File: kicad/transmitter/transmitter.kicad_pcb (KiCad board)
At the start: 2 copper layers, 69.9 x 43.2 mm, 30 parts, among them J1 Conn_01x02, J2 Conn_01x04, J3 AudioJack3, J4 AudioJack3, SW1 SW_SPST, SW2 SW_SPST, U1 ATmega328P-PU, U2 NRF24L01_Breakout, U3 MH-M18, U4 MSGEQ7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

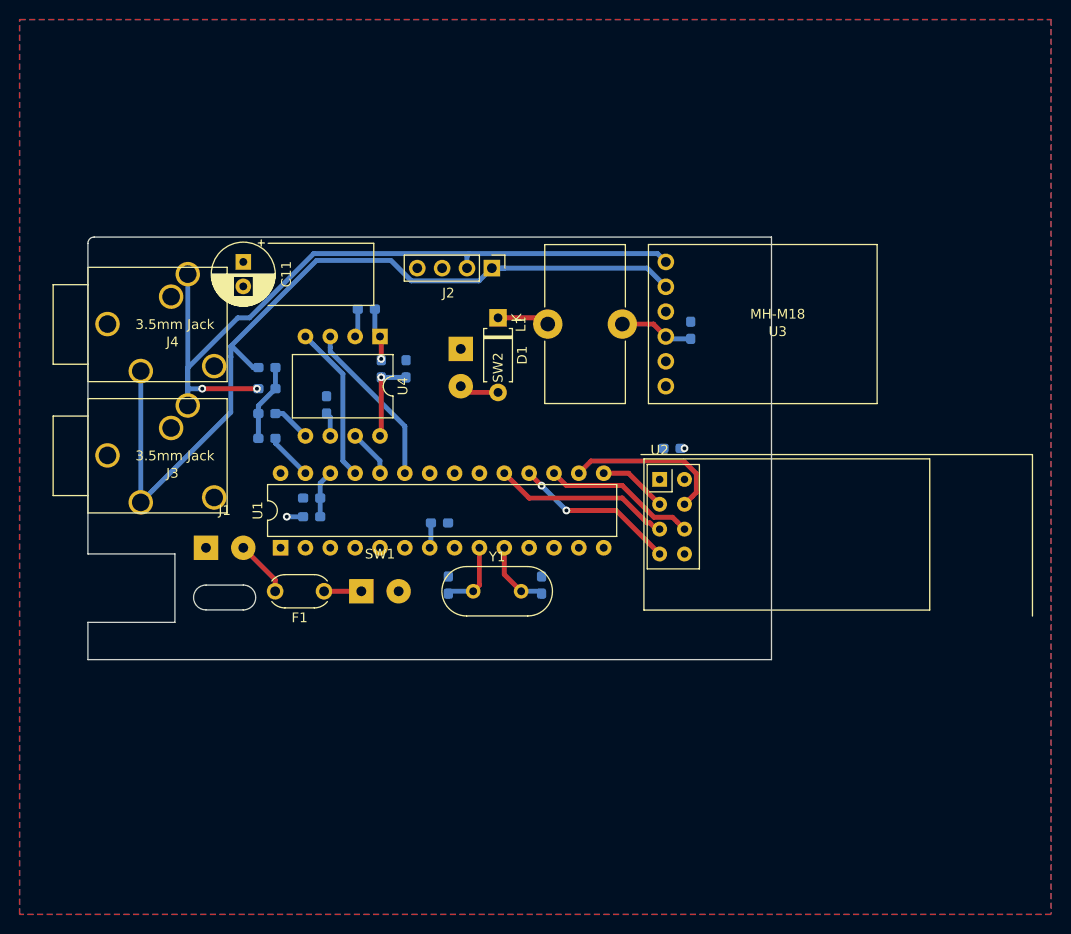
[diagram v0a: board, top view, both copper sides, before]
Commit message: Button, LEDs, ICSP header
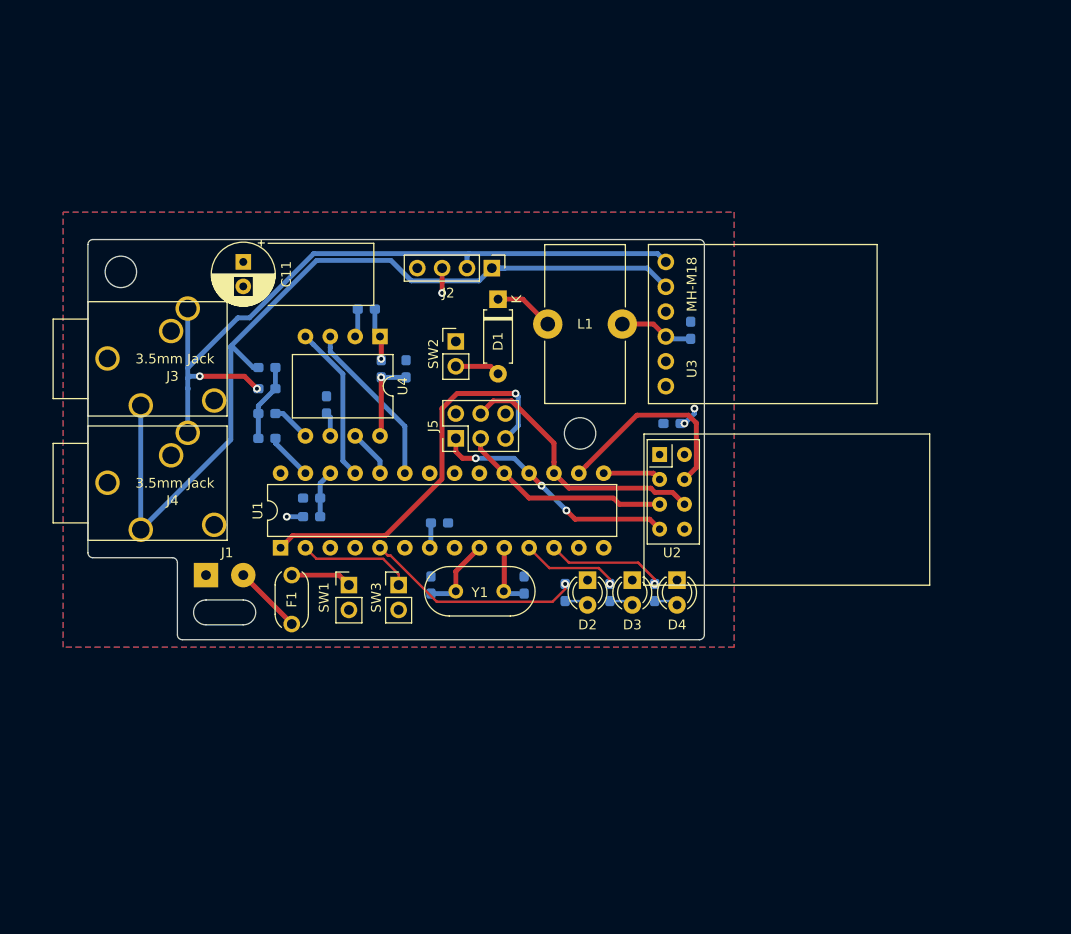
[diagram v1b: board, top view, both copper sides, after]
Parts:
- added D2: LED, LED_THT:LED_D3.0mm, F.Cu at (129.8, 87.1)
- added D3: LED, LED_THT:LED_D3.0mm, F.Cu at (134.4, 87.1)
- added D4: LED, LED_THT:LED_D3.0mm, F.Cu at (138.9, 87.1)
- added J5: Conn_02x03_Odd_Even, Connector_PinHeader_2.54mm:PinHeader_2x03_P2.54mm_Vertical, F.Cu at (116.3, 72.6)
- added R6: R, Resistor_SMD:R_0603_1608Metric_Pad1.05x0.95mm_HandSolder, B.Cu at (127.5, 88.4)
- added R7: R, Resistor_SMD:R_0603_1608Metric_Pad1.05x0.95mm_HandSolder, B.Cu at (132.1, 88.4)
- added R8: R, Resistor_SMD:R_0603_1608Metric_Pad1.05x0.95mm_HandSolder, B.Cu at (136.7, 88.4)
- added SW3: SW_Push, Connector_PinHeader_2.54mm:PinHeader_1x02_P2.54mm_Vertical, F.Cu at (110.5, 87.6)
- SW1, SW2: footprint Connector_Wire:SolderWirePad_1x02_P3.81mm_Drill1mm -> Connector_PinHeader_2.54mm:PinHeader_1x02_P2.54mm_Vertical
- moved J4 16.2 mm to (78.7, 71.4)
- moved J3 9.91 mm to (78.7, 58.7)
- moved F1 3.69 mm to (99.6, 86.6), turned to 270 degrees
- moved J1 2.79 mm to (90.8, 86.6)
- moved C4 2.54 mm to (138.4, 71.1)
- moved U2 2.54 mm to (137.2, 74.3)
- moved D1 1.91 mm to (120.7, 58.4)
- moved C3 1.78 mm to (123.3, 87.6)
- moved Y1 1.78 mm to (116.3, 88.3)
- moved C2 1.78 mm to (113.8, 87.6)
- moved SW1 1.42 mm to (105.4, 87.6)
- moved SW2 0.92 mm to (116.3, 62.7), turned to 0 degrees
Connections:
- net Radio3 renamed MOSI
- net Radio4 renamed MISO
- U1 pad 1: Net-(U1-Pad1) -> RST
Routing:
- net RST: track 0.00 -> 40.0 mm, vias 0 -> 1
- net Net-(R6-Pad1): track 0.00 -> 22.4 mm, vias 0 -> 1
- net Net-(R8-Pad1): track 0.00 -> 12.1 mm, vias 0 -> 1
- net MOSI: track 15.7 -> 27.5 mm
- net Net-(SW3-Pad1): track 0.00 -> 11.7 mm
- net Net-(R7-Pad1): track 0.00 -> 10.1 mm, vias 0 -> 1
- net MISO: track 16.8 -> 25.5 mm, vias 2 -> 3
- net Radio2: track 16.7 -> 21.1 mm
- net Net-(J2-Pad2): track 80.1 -> 76.2 mm
- net Radio5: track 18.2 -> 22.1 mm
- net GND: track 2.91 -> 5.45 mm, vias 0 -> 1
- net Net-(F1-Pad1): track 3.81 -> 6.26 mm
- net Net-(D2-Pad2): track 0.00 -> 2.45 mm
- net Net-(D4-Pad2): track 0.00 -> 2.45 mm
- net Net-(D3-Pad2): track 0.00 -> 2.45 mm
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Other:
- board size 69.9 x 43.2 mm -> 63 x 40.9 mm

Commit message: Tidy-ups pre-order
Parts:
- added REF**: OSHW-Logo2_9.8x8mm_SilkScreen, Symbol:OSHW-Logo2_9.8x8mm_SilkScreen, B.Cu at (129.5, 65.5)
- added REF**: OSHW-Logo2_9.8x8mm_SilkScreen, Symbol:OSHW-Logo2_9.8x8mm_SilkScreen, F.Cu at (0.00, 0.00)
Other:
- board size 63 x 40.9 mm -> 63 x 40.6 mm
- board text added: "Audio Lighting Transmitter v1.0 Damian Moore 2020"

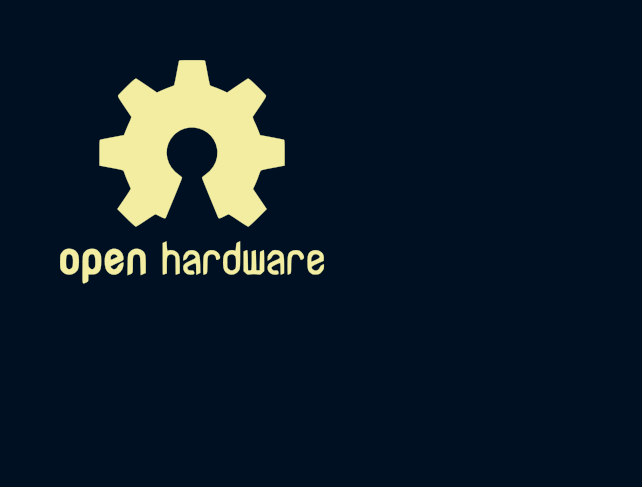
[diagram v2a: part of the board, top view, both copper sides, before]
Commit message: Removes unused silkscreen symbol from PCB
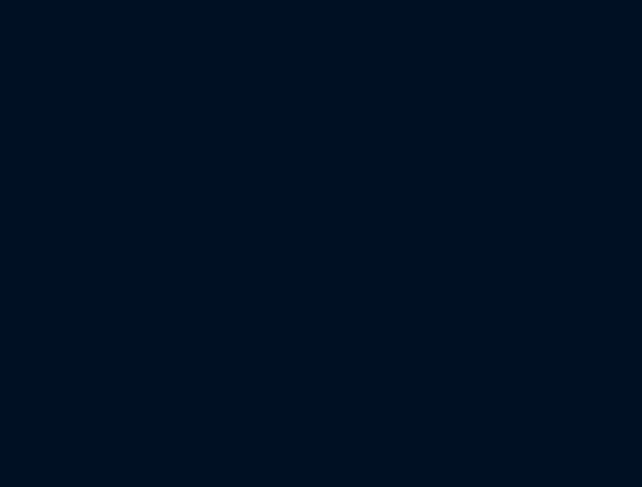
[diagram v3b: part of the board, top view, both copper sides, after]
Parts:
- removed the REF** at (0.00, 0.00)
